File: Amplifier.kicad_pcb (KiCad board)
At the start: 2 copper layers, 50.5 x 65.5 mm, 32 parts, among them J1 Conn_01x02, J2 Conn_01x02, J3 Conn_01x02, Q1 2N3904, Q2 2N3904, Q3 2N3906, U1 NE5532

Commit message: mid layout check-in
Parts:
- C1, C2, C3, C4, C5, C6: footprint Capacitor_THT:C_Rect_L7.0mm_W2.0mm_P5.00mm -> Capacitor_THT:C_Rect_L7.0mm_W2.5mm_P5.00mm
- C10: footprint Capacitor_THT:C_Rect_L7.0mm_W2.0mm_P5.00mm -> Capacitor_THT:CP_Radial_D10.0mm_P5.00mm
- C11, C8, C9: footprint Capacitor_THT:CP_Radial_D6.3mm_P2.50mm -> Capacitor_THT:CP_Radial_D10.0mm_P5.00mm
- C7: footprint Capacitor_THT:C_Rect_L7.0mm_W2.0mm_P5.00mm -> Capacitor_THT:CP_Radial_D8.0mm_P3.50mm
- J1: footprint Connector_PinHeader_2.54mm:PinHeader_1x02_P2.54mm_Vertical -> TerminalBlock:TerminalBlock_Altech_AK300-2_P5.00mm
- J2, J3: footprint Connector_Wire:SolderWire-0.75sqmm_1x02_P4.8mm_D1.25mm_OD2.3mm -> TerminalBlock:TerminalBlock_Altech_AK300-2_P5.00mm
- Q1, Q2, Q3: footprint Package_TO_SOT_THT:TO-92_Inline -> Package_TO_SOT_THT:TO-92_Inline_Wide
- R1, R10, R11, R12, R13, R14, R2, R3, R4, R5, R6, R7, R8, R9: footprint Resistor_THT:R_Axial_DIN0204_L3.6mm_D1.6mm_P7.62mm_Horizontal -> Resistor_THT:R_Axial_DIN0207_L6.3mm_D2.5mm_P10.16mm_Horizontal
- moved R14 141.0 mm to (162.6, 79.4)
- moved R13 138.2 mm to (157.5, 90.0), turned to 180 degrees
- moved J3 134.9 mm to (177.8, 91.0), turned to 90 degrees
- moved R12 128.2 mm to (147.3, 86.4)
- moved Q1 125.0 mm to (142.2, 86.4), turned to 90 degrees
- moved Q3 121.1 mm to (141.9, 90.2), turned to -90 degrees
- moved R6 120.8 mm to (118.1, 112.4)
- moved R9 117.2 mm to (136.5, 74.9), turned to 180 degrees
- moved R10 115.5 mm to (136.5, 68.6), turned to 180 degrees
- moved R7 114.6 mm to (123.8, 95.2), turned to -90 degrees
- moved C11 113.0 mm to (162.6, 88.3)
- moved Q2 111.9 mm to (131.4, 84.5)
- moved R1 109.9 mm to (91.4, 108.6)
- moved C9 109.6 mm to (148.8, 98.4)
- moved R8 107.4 mm to (126.4, 71.8)
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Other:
- board outline removed

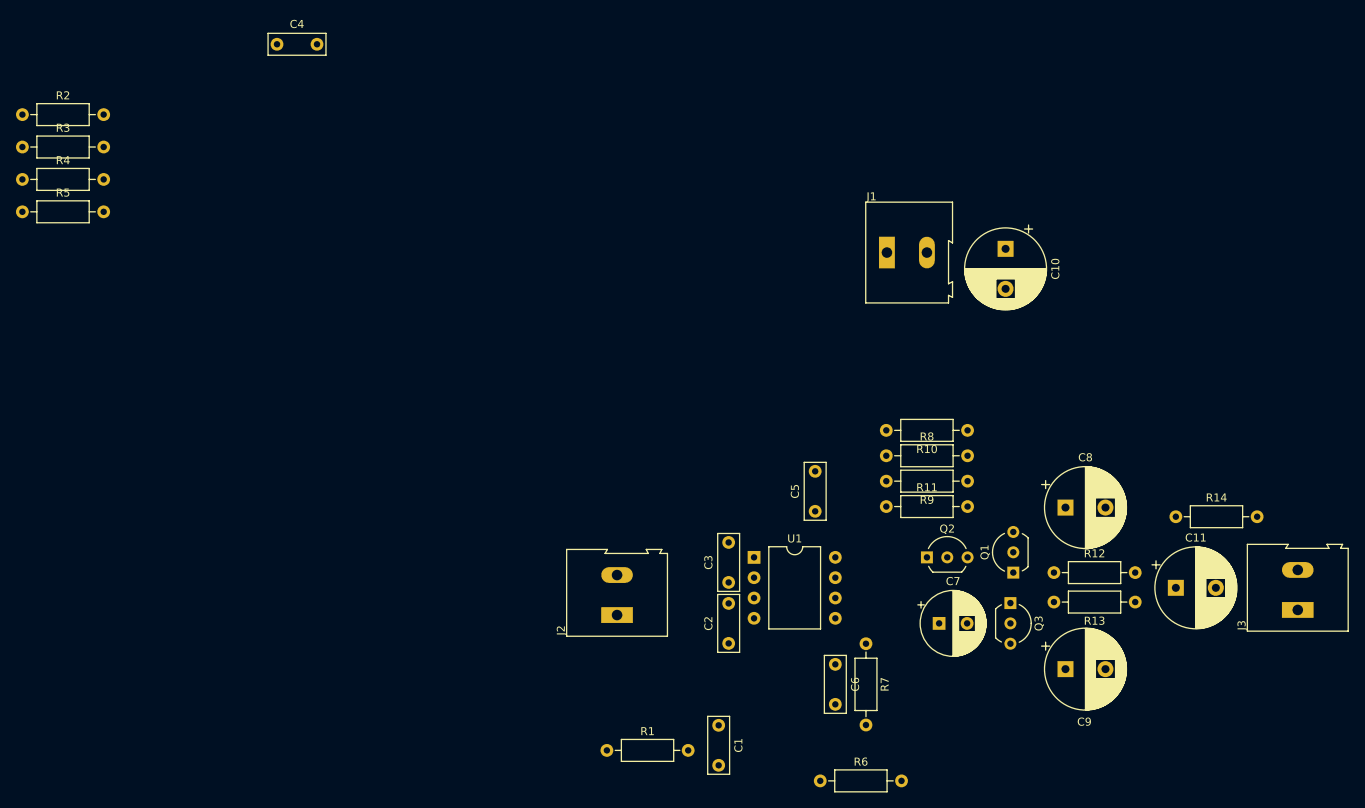
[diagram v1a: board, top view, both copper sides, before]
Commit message: layout work and added M3 mounting holes
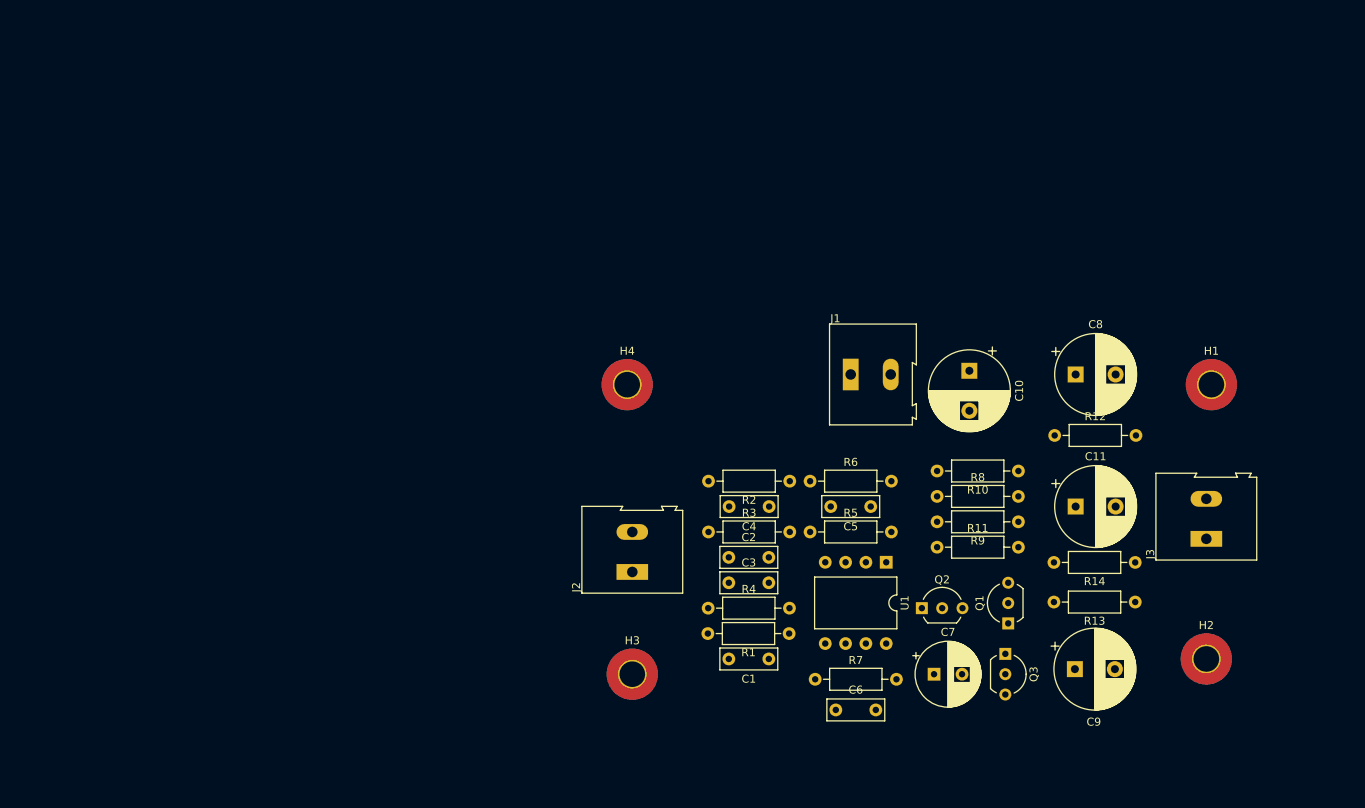
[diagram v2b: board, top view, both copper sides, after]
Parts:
- added H1: MountingHole_Pad, MountingHole:MountingHole_3.2mm_M3_Pad_TopBottom, F.Cu at (167.0, 62.9)
- added H2: MountingHole_Pad, MountingHole:MountingHole_3.2mm_M3_Pad_TopBottom, F.Cu at (166.4, 97.2)
- added H3: MountingHole_Pad, MountingHole:MountingHole_3.2mm_M3_Pad_TopBottom, F.Cu at (94.6, 99.1)
- added H4: MountingHole_Pad, MountingHole:MountingHole_3.2mm_M3_Pad_TopBottom, F.Cu at (94.0, 62.9)
- moved R2 106.3 mm to (114.3, 74.9), turned to 180 degrees
- moved R5 106.3 mm to (116.8, 81.3)
- moved R4 101.1 mm to (104.1, 90.8)
- moved R3 98.3 mm to (104.1, 81.3)
- moved C4 84.4 mm to (111.7, 78.1), turned to 180 degrees
- moved R6 37.5 mm to (116.8, 74.9)
- moved R1 27.1 mm to (114.2, 94.0), turned to 180 degrees
- moved R12 17.1 mm to (147.4, 69.2)
- moved C8 16.7 mm to (150.0, 61.6)
- moved U1 16.5 mm to (126.4, 85.1), turned to -90 degrees
- moved C11 16.1 mm to (150.0, 78.1)
- moved C10 15.9 mm to (136.8, 61.1)
- moved J1 15.9 mm to (121.9, 61.6)
- moved J3 14.5 mm to (166.4, 82.1)
- moved C2 10.8 mm to (106.7, 84.5), turned to 0 degrees
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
